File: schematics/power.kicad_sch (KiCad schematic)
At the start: 8 parts, among them U2 RT9193-33GB

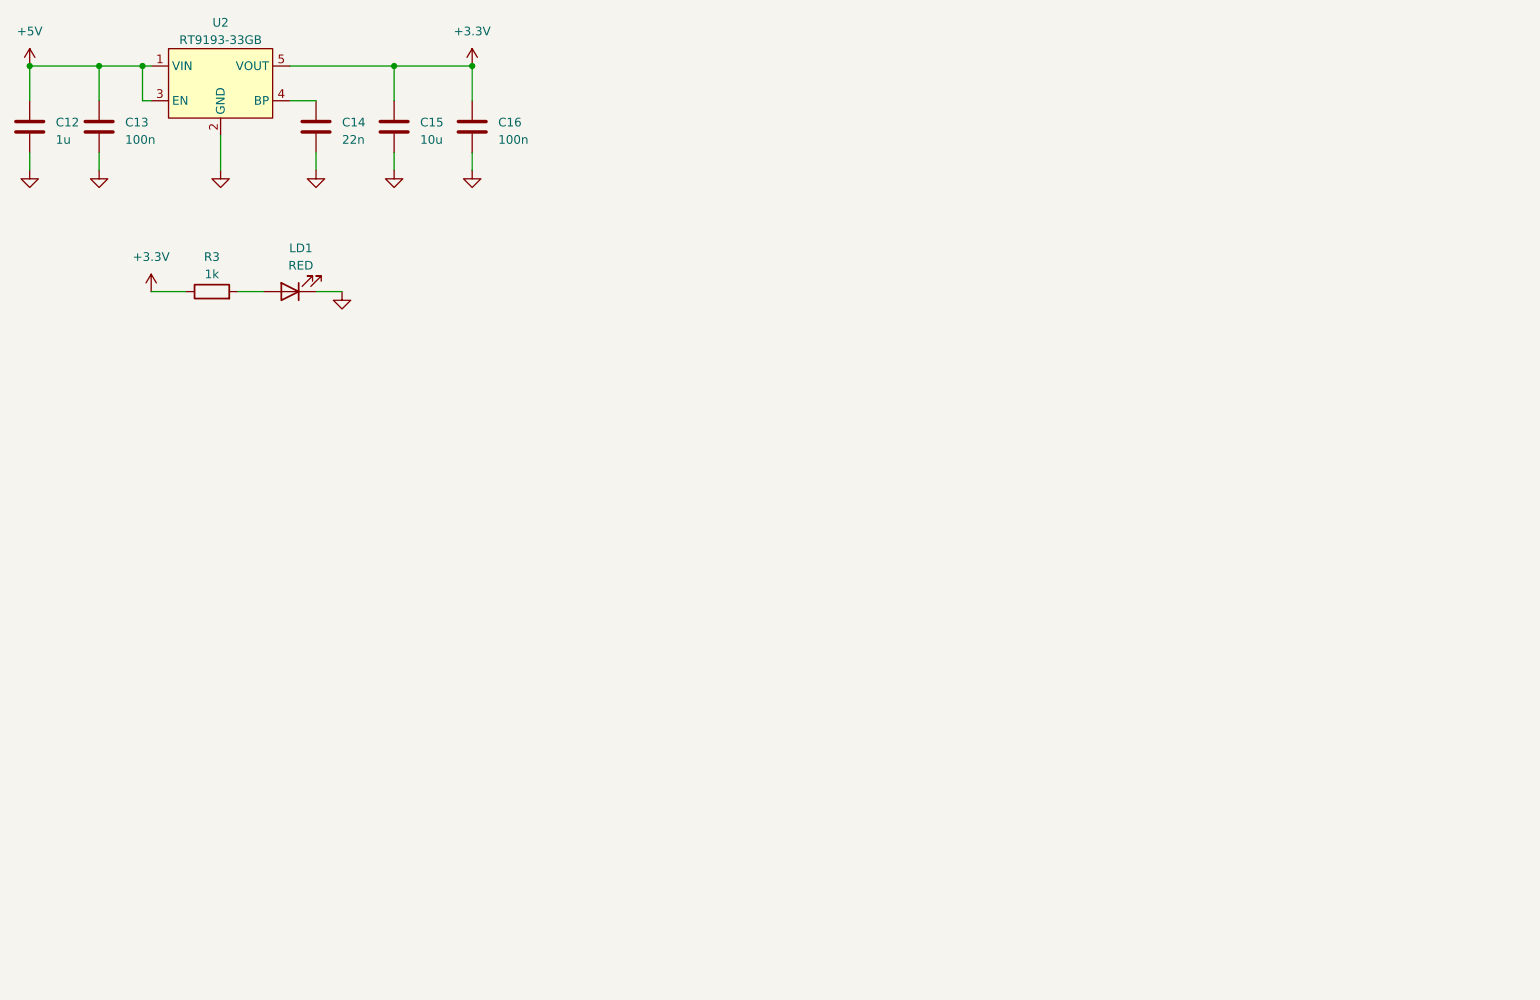
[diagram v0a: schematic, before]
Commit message: Обновил файлы и добавил новые элемнты
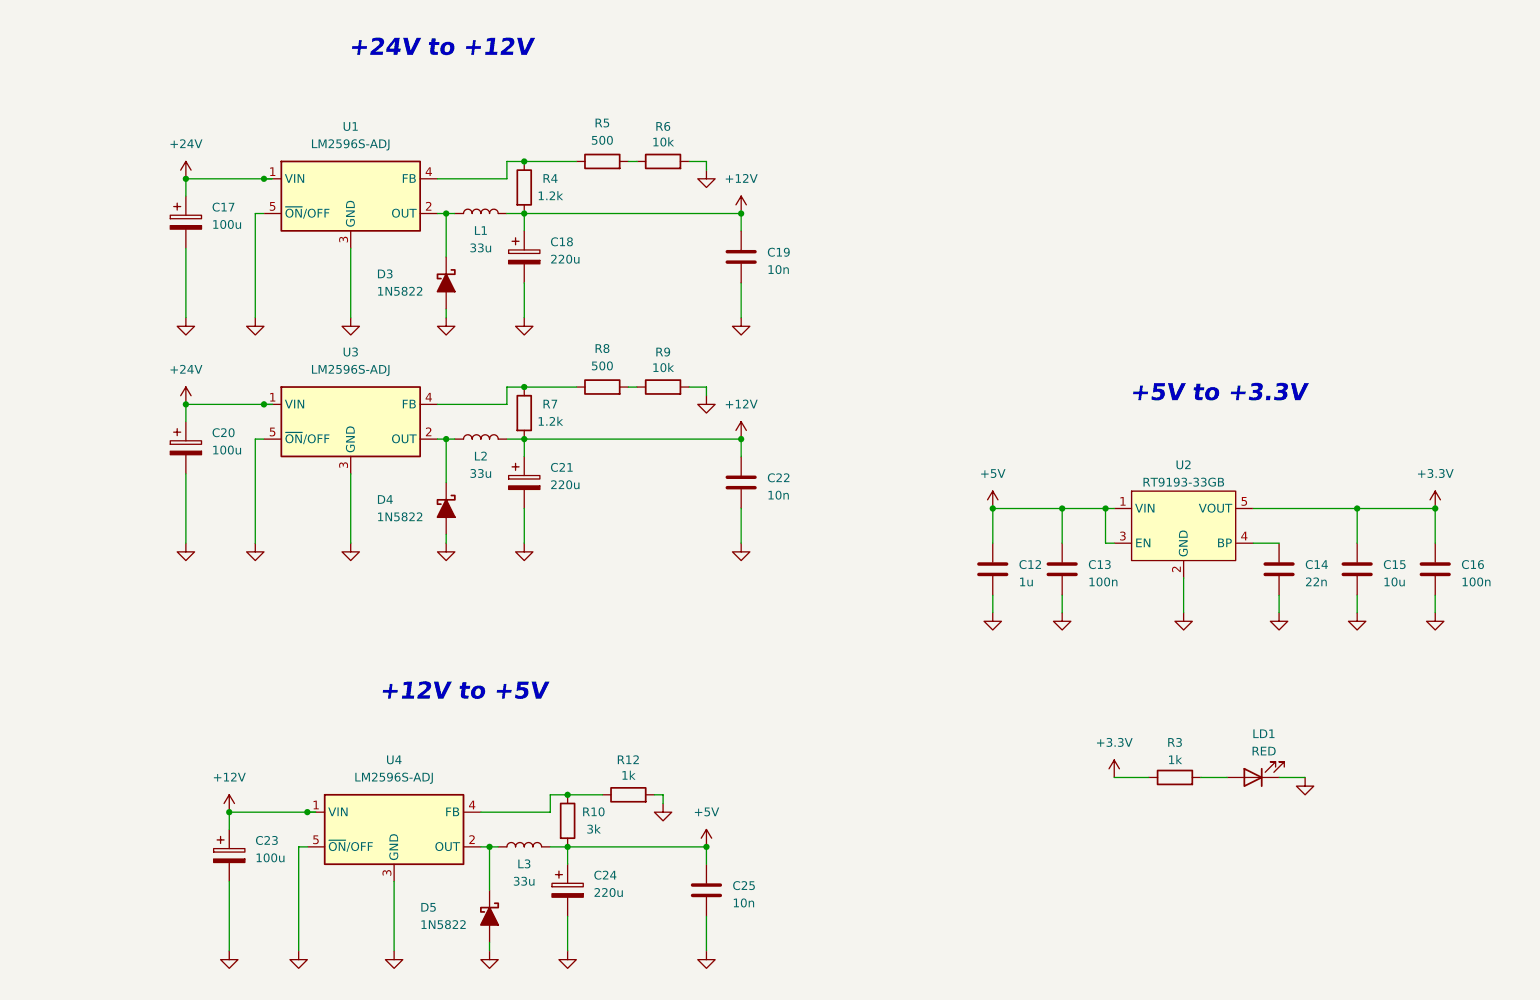
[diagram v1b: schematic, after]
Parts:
- added C17, C20, C23: 100u, symbol Device:C_Polarized
- added C18, C21, C24: 220u, symbol Device:C_Polarized
- added C19, C22, C25: 10n, Capacitor_SMD:C_1206_3216Metric_Pad1.33x1.80mm_HandSolder, symbol Device:C
- added D3, D4, D5: 1N5822, PCM_4ms_Diode:D_DO-214AC_SMA, symbol PCM_Diode_Schottky_AKL:1N5822
- added L1, L2, L3: 33u, Inductor_SMD:L_Bourns_SRR1260, symbol Device:L
- added R10: 3k, Resistor_SMD:R_1206_3216Metric_Pad1.30x1.75mm_HandSolder, symbol Device:R
- added R12: 1k, Resistor_SMD:R_1206_3216Metric_Pad1.30x1.75mm_HandSolder, symbol Device:R
- added R4, R7: 1.2k, Resistor_SMD:R_1206_3216Metric_Pad1.30x1.75mm_HandSolder, symbol Device:R
- added R5, R8: 500, Resistor_SMD:R_1206_3216Metric_Pad1.30x1.75mm_HandSolder, symbol Device:R
- added R6, R9: 10k, Resistor_SMD:R_1206_3216Metric_Pad1.30x1.75mm_HandSolder, symbol Device:R
- added U1, U3, U4: LM2596S-ADJ, Package_TO_SOT_SMD:TO-263-5_TabPin3, symbol Regulator_Switching:LM2596S-ADJ
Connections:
- net +5V: now also C24.1, C25.2, L3.2, R10.2
- net GND: now also C17.2, C18.2, C19.1, C20.2, C21.2, C22.1, C23.2, C24.2, C25.1, D3.2 (A), D4.2 (A), D5.2 (A), R12.2, R6.2, R9.2, U1.3 (GND), U1.5 (~{ON}/OFF), U3.3 (GND), U3.5 (~{ON}/OFF), U4.3 (GND), U4.5 (~{ON}/OFF)
- new net: R4.1, R5.1, U1.4 (FB)
- new net: D3.1 (K), L1.1, U1.2 (OUT)
- new net: R8.2, R9.1
- new net: D4.1 (K), L2.1, U3.2 (OUT)
- new net: D5.1 (K), L3.1, U4.2 (OUT)
- new net: R10.1, R12.1, U4.4 (FB)
- new net: R5.2, R6.1
- new net: R7.1, R8.1, U3.4 (FB)
- new net +12V: C18.1, C19.2, C21.1, C22.2, C23.1, L1.2, L2.2, R4.2, R7.2, U4.1 (VIN)
- new net +24V: C17.1, C20.1, U1.1 (VIN), U3.1 (VIN)
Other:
- note added: "+12V to +5V"
- note added: "+24V to +12V"
- note added: "+5V to +3.3V"
- moved on the sheet: C12, C13, C14, C15, C16, LD1, R3, U2

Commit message: Файлы измененный Kicad
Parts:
- added LD9901, LD9902, LD9903: ~, LED_SMD:LED_1206_3216Metric_Pad1.42x1.75mm_HandSolder, symbol Device:LED
- added R9909, R9910, R9911: 1k, Resistor_SMD:R_1206_3216Metric_Pad1.30x1.75mm_HandSolder, symbol Device:R
- C9900: renamed from C17; footprint (none) -> Capacitor_SMD:C_0805_2012Metric
- C9901: renamed from C18; footprint (none) -> Capacitor_SMD:C_0805_2012Metric
- C9902: renamed from C19; footprint Capacitor_SMD:C_1206_3216Metric_Pad1.33x1.80mm_HandSolder -> Capacitor_SMD:C_0805_2012Metric
- C9903: renamed from C20; footprint (none) -> Capacitor_SMD:C_0805_2012Metric
- C9904: renamed from C21; footprint (none) -> Capacitor_SMD:C_0805_2012Metric
- C9905: renamed from C22; footprint Capacitor_SMD:C_1206_3216Metric_Pad1.33x1.80mm_HandSolder -> Capacitor_SMD:C_0805_2012Metric
- C9906: renamed from C23; footprint (none) -> Capacitor_SMD:C_0805_2012Metric
- C9907: renamed from C24; footprint (none) -> Capacitor_SMD:C_0805_2012Metric
- C9908: renamed from C25; footprint Capacitor_SMD:C_1206_3216Metric_Pad1.33x1.80mm_HandSolder -> Capacitor_SMD:C_0805_2012Metric
- C9909: renamed from C12; footprint Capacitor_SMD:C_1206_3216Metric_Pad1.33x1.80mm_HandSolder -> Capacitor_SMD:C_0805_2012Metric
- C9910: renamed from C13; footprint Capacitor_SMD:C_1206_3216Metric_Pad1.33x1.80mm_HandSolder -> Capacitor_SMD:C_0805_2012Metric
- C9911: renamed from C14; footprint Capacitor_SMD:C_1206_3216Metric_Pad1.33x1.80mm_HandSolder -> Capacitor_SMD:C_0805_2012Metric
- C9912: renamed from C15; footprint Capacitor_SMD:C_1206_3216Metric_Pad1.33x1.80mm_HandSolder -> Capacitor_SMD:C_0805_2012Metric
- C9913: renamed from C16; footprint Capacitor_SMD:C_1206_3216Metric_Pad1.33x1.80mm_HandSolder -> Capacitor_SMD:C_0805_2012Metric
- LD9900: renamed from LD1; value RED -> ~
- U10: renamed from U3; footprint Package_TO_SOT_SMD:TO-263-5_TabPin3 -> PCM_Package_TO_SOT_SMD_AKL:TO-263-5_TabPin3_ThermalVias
- U11: renamed from U4; footprint Package_TO_SOT_SMD:TO-263-5_TabPin3 -> PCM_Package_TO_SOT_SMD_AKL:TO-263-5_TabPin3_ThermalVias
- U9: renamed from U1; footprint Package_TO_SOT_SMD:TO-263-5_TabPin3 -> PCM_Package_TO_SOT_SMD_AKL:TO-263-5_TabPin3_ThermalVias
- renumbered D3 to D9900, D4 to D9901, D5 to D9902, L1 to L9900, L2 to L9901, L3 to L9902, R4 to R9900, R5 to R9901, R6 to R9902, R7 to R9903, R8 to R9904, R9 to R9905, R10 to R9906, R12 to R9907, R3 to R9908, U2 to U12
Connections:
- net +12V: now also R9910.1
- net +24V: now also R9911.1
- net +5V: now also R9909.1
- net GND: now also LD9901.1 (K), LD9902.1 (K), LD9903.1 (K)
- new net: LD9902.2 (A), R9910.2
- new net: LD9901.2 (A), R9909.2
- new net: LD9903.2 (A), R9911.2
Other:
- moved on the sheet: C9909, C9910, C9911, C9912, C9913, R9908, U12

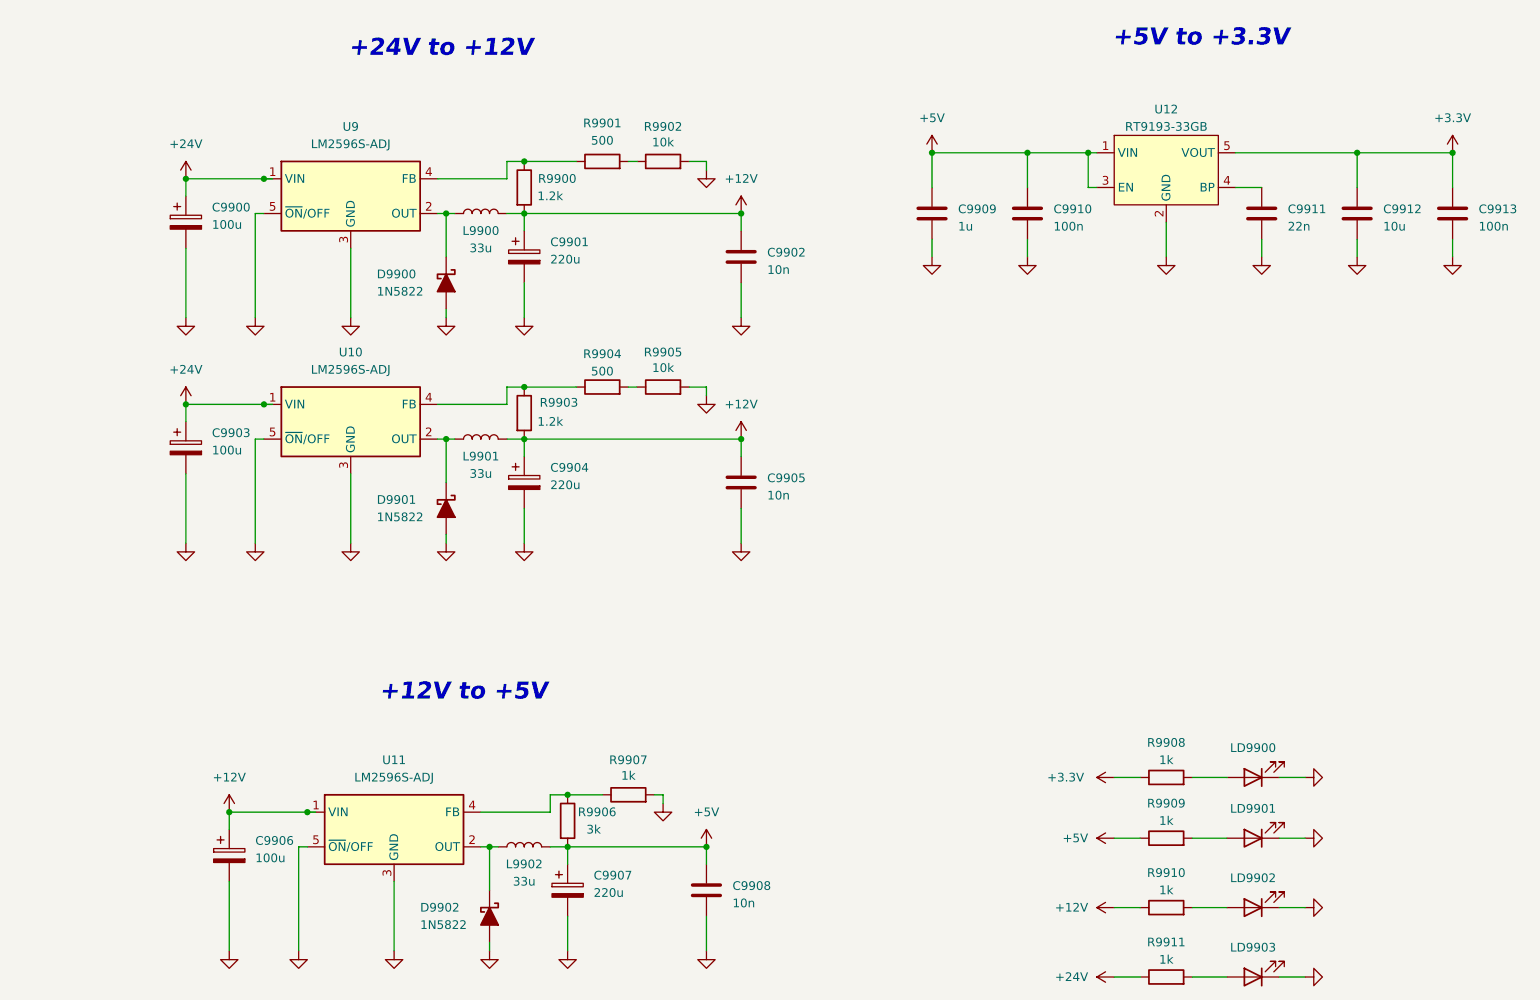
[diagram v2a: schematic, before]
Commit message: Прошелся по всей схеме: 1. почистил компоненты; 2. задал посадочные места; 3. Выставил все ссылки на плате в притык, дальнейшее расширение - смена мк
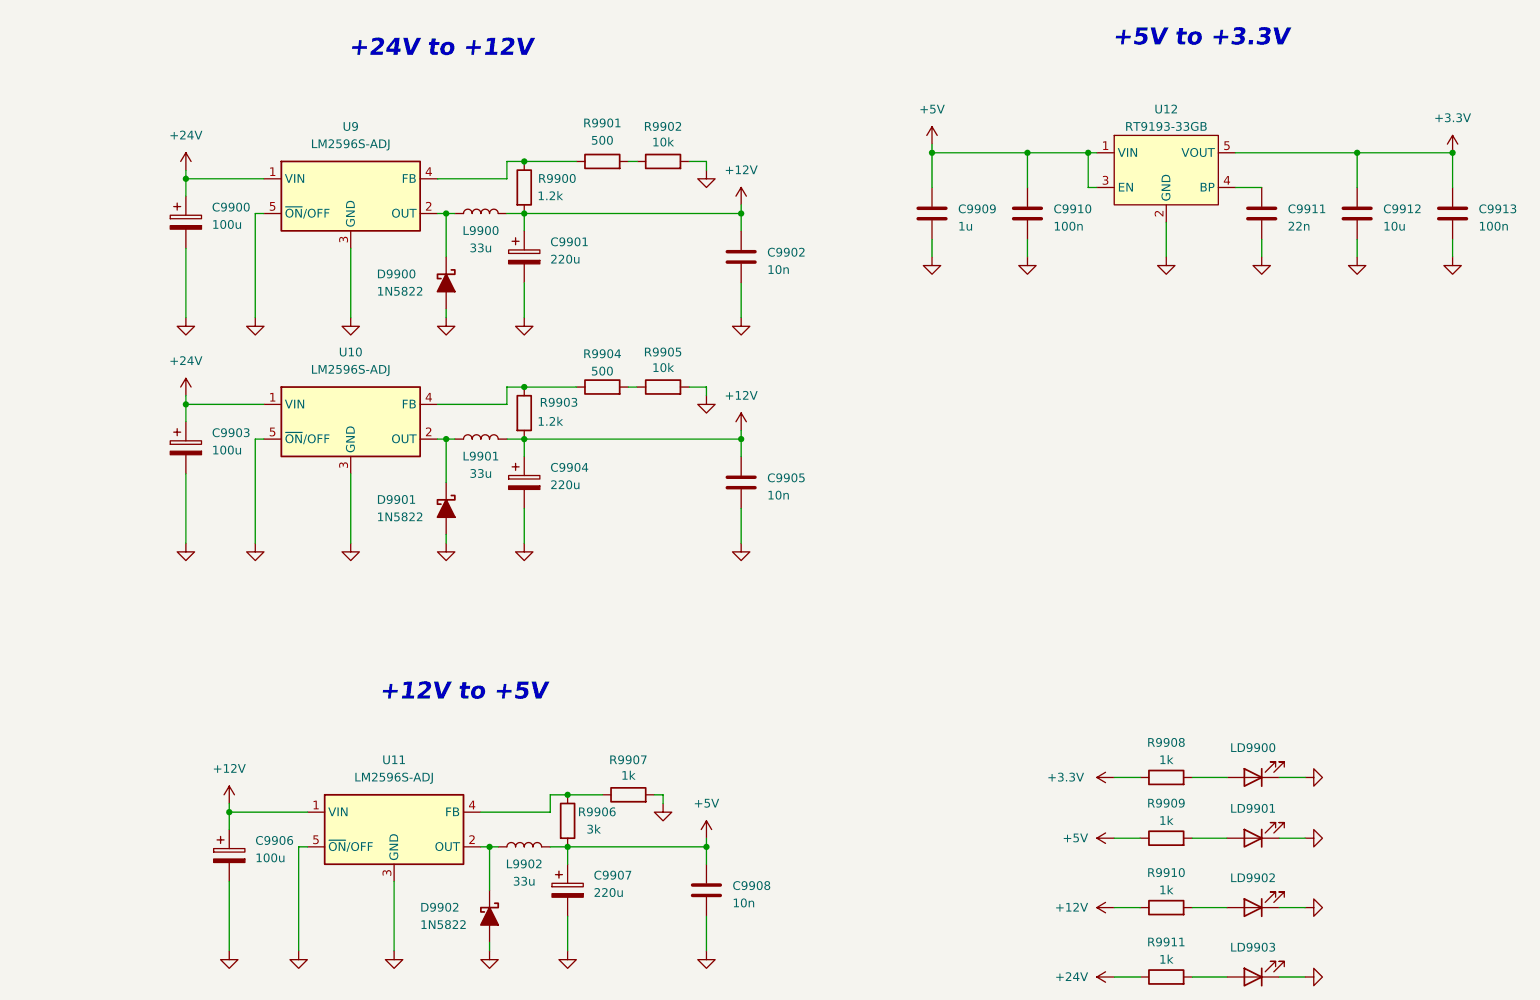
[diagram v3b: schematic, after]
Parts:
- L9900, L9901, L9902: footprint Inductor_SMD:L_Bourns_SRR1260 -> Inductor_SMD:L_APV_APH0650
- LD9900, LD9901, LD9902, LD9903: footprint LED_SMD:LED_1206_3216Metric_Pad1.42x1.75mm_HandSolder -> LED_SMD:LED_0805_2012Metric
- R9900, R9901, R9902, R9903, R9904, R9905, R9906, R9907, R9908, R9909, R9910, R9911: footprint Resistor_SMD:R_1206_3216Metric_Pad1.30x1.75mm_HandSolder -> Resistor_SMD:R_0805_2012Metric
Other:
- company: (none) -> Филимонов и К

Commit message: Не корректно посадочное место выбрал
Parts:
- added PWR0: Conn_01x02, Connector_Phoenix_MC:PhoenixContact_MC_1,5_2-G-3.81_1x02_P3.81mm_Horizontal, symbol Connector_Generic:Conn_01x02
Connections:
- net +24V: now also PWR0.1 (Pin_1)
- net GND: now also PWR0.2 (Pin_2)
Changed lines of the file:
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@@
 	(wire
 		(pts
+			(xy 204.47 91.44) (xy 207.01 91.44)
+		)
+		(stroke
+			(width 0)
+			(type default)
+		)
+	)
+	(wire
+		(pts
 			(xy 109.22 82.55) (xy 111.76 82.55)
 		)
@@
 	(wire
 		(pts
+			(xy 204.47 93.98) (xy 207.01 93.98)
+		)
+		(stroke
+			(width 0)
+			(type default)
+		)
+	)
+	(wire
+		(pts
 			(xy 118.11 144.78) (xy 118.11 142.24)
 		)
@@
 	)
 	(symbol
+		(lib_id "Connector_Generic:Conn_01x02")
+		(at 212.09 91.44 0)
+		(unit 1)
+		(exclude_from_sim no)
+		(in_bom yes)
+		(on_board yes)
+		(dnp no)
+		(fields_autoplaced yes)
+		(property "Reference" "PWR0"
+			(at 214.63 91.4399 0)
+			(effects
+				(font
+					(size 1.27 1.27)
+				)
+				(justify left)
+			)
+		)
+		(property "Value" "Conn_01x02"
+			(at 214.63 93.9799 0)
+			(effects
+				(font
+					(size 1.27 1.27)
+				)
+				(justify left)
+				(hide yes)
+			)
+		)
+		(property "Footprint" "Connector_Phoenix_MC:PhoenixContact_MC_1,5_2-G-3.81_1x02_P3.81mm_Horizontal"
+			(at 212.09 91.44 0)
+			(effects
+				(font
+					(size 1.27 1.27)
+				)
+				(hide yes)
+			)
+		)
+		(property "Datasheet" "~"
+			(at 212.09 91.44 0)
+			(effects
+				(font
+					(size 1.27 1.27)
+				)
+				(hide yes)
+			)
+		)
+		(property "Description" "Generic connector, single row, 01x02, script generated (kicad-library-utils/schlib/autogen/connector/)"
+			(at 212.09 91.44 0)
+			(effects
+				(font
+					(size 1.27 1.27)
+				)
+				(hide yes)
+			)
+		)
+		(pin "1"
+		)
+		(pin "2"
+		)
+		(instances
+			(project ""
+				(path "/97e8f341-b455-4614-ab7f-cc310164e7aa/7330fb6d-3de7-4c19-a7a3-dd8fb4865426"
+					(reference "PWR0")
+					(unit 1)
+				)
+			)
+		)
+	)
+	(symbol
 		(lib_id "power:GND")
 		(at 118.11 157.48 0)
@@
 	)
 	(symbol
+		(lib_id "power:+24V")
+		(at 204.47 91.44 0)
+		(unit 1)
+		(exclude_from_sim no)
+		(in_bom yes)
+		(on_board yes)
+		(dnp no)
+		(fields_autoplaced yes)
+		(property "Reference" "#PWR0238"
+			(at 204.47 95.25 0)
+			(effects
+				(font
+					(size 1.27 1.27)
+				)
+				(hide yes)
+			)
+		)
+		(property "Value" "+24V"
+			(at 204.47 86.36 0)
+			(effects
+				(font
+					(size 1.27 1.27)
+				)
+			)
+		)
+		(property "Footprint" ""
+			(at 204.47 91.44 0)
+			(effects
+				(font
+					(size 1.27 1.27)
+				)
+				(hide yes)
+			)
+		)
+		(property "Datasheet" ""
+			(at 204.47 91.44 0)
+			(effects
+				(font
+					(size 1.27 1.27)
+				)
+				(hide yes)
+			)
+		)
+		(property "Description" "Power symbol creates a global label with name \"+24V\""
+			(at 204.47 91.44 0)
+			(effects
+				(font
+					(size 1.27 1.27)
+				)
+				(hide yes)
+			)
+		)
+		(pin "1"
+		)
+		(instances
+			(project "MasterBoard"
+				(path "/97e8f341-b455-4614-ab7f-cc310164e7aa/7330fb6d-3de7-4c19-a7a3-dd8fb4865426"
+					(reference "#PWR0238")
+					(unit 1)
+				)
+			)
+		)
+	)
+	(symbol
 		(lib_id "Device:R")
 		(at 111.76 78.74 0)
@@
 					(unit 1)
 				)
+			)
+		)
+	)
+	(symbol
+		(lib_id "power:GND")
+		(at 204.47 93.98 0)
+		(unit 1)
+		(exclude_from_sim no)
+		(in_bom yes)
+		(on_board yes)
+		(dnp no)
+		(fields_autoplaced yes)
+		(property "Reference" "#PWR0239"
+			(at 204.47 100.33 0)
+			(effects
+				(font
+					(size 1.27 1.27)
+				)
+				(hide yes)
+			)
+		)
+		(property "Value" "GND"
+			(at 204.47 99.06 0)
+			(effects
+				(font
+					(size 1.27 1.27)
+				)
+				(hide yes)
+			)
+		)
+		(property "Footprint" ""
+			(at 204.47 93.98 0)
+			(effects
+				(font
+					(size 1.27 1.27)
+				)
+				(hide yes)
+			)
+		)
+		(property "Datasheet" ""
+			(at 204.47 93.98 0)
+			(effects
+				(font
+					(size 1.27 1.27)
+				)
+				(hide yes)
+			)
+		)
+		(property "Description" "Power symbol creates a global label with name \"GND\" , ground"
+			(at 204.47 93.98 0)
+			(effects
+				(font
+					(size 1.27 1.27)
+				)
+				(hide yes)
+			)
+		)
+		(pin "1"
+		)
+		(instances
+			(project "MasterBoard"
+				(path "/97e8f341-b455-4614-ab7f-cc310164e7aa/7330fb6d-3de7-4c19-a7a3-dd8fb4865426"
+					(reference "#PWR0239")
+					(unit 1)
+				)
